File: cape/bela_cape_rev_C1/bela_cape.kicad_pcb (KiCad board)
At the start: 4 copper layers, 127 parts, among them IC1 TLV320AIC3104, IC2 MIC5317, IC3 ES9080Q, IC4 LM4876, IC5 LM4876, IC6 TSV524xIQ4T, IC7 TSV524xIQ4T, IC8 ADS8168, J1 Conn_01x02, J10 Conn_01x04, J11 Conn_01x02, J2 Conn_01x04, J3 Conn_01x03, J4 Conn_01x03, J5 Conn_01x02, J6 Conn_01x02, J7 Conn_01x10, J8 Conn_01x10, J9 Conn_01x04, P1 BeagleBone_Black_Header, U1 TL974, U2 TL974

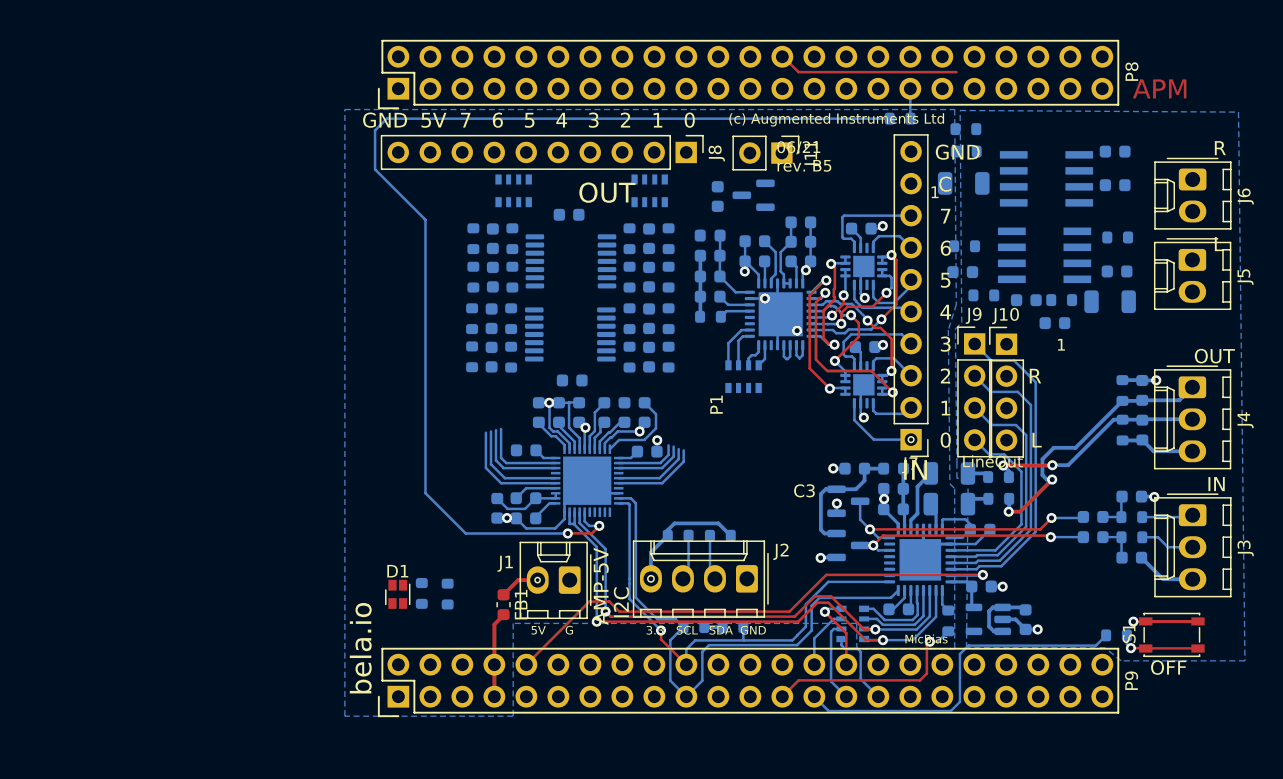
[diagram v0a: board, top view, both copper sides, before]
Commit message: Updates to Bela cape C1, adding 3-pin connectors for raw analog out
(cherry picked from commit eb88a9ebe73bf9c3f735ce6d0fd609408781e91a)
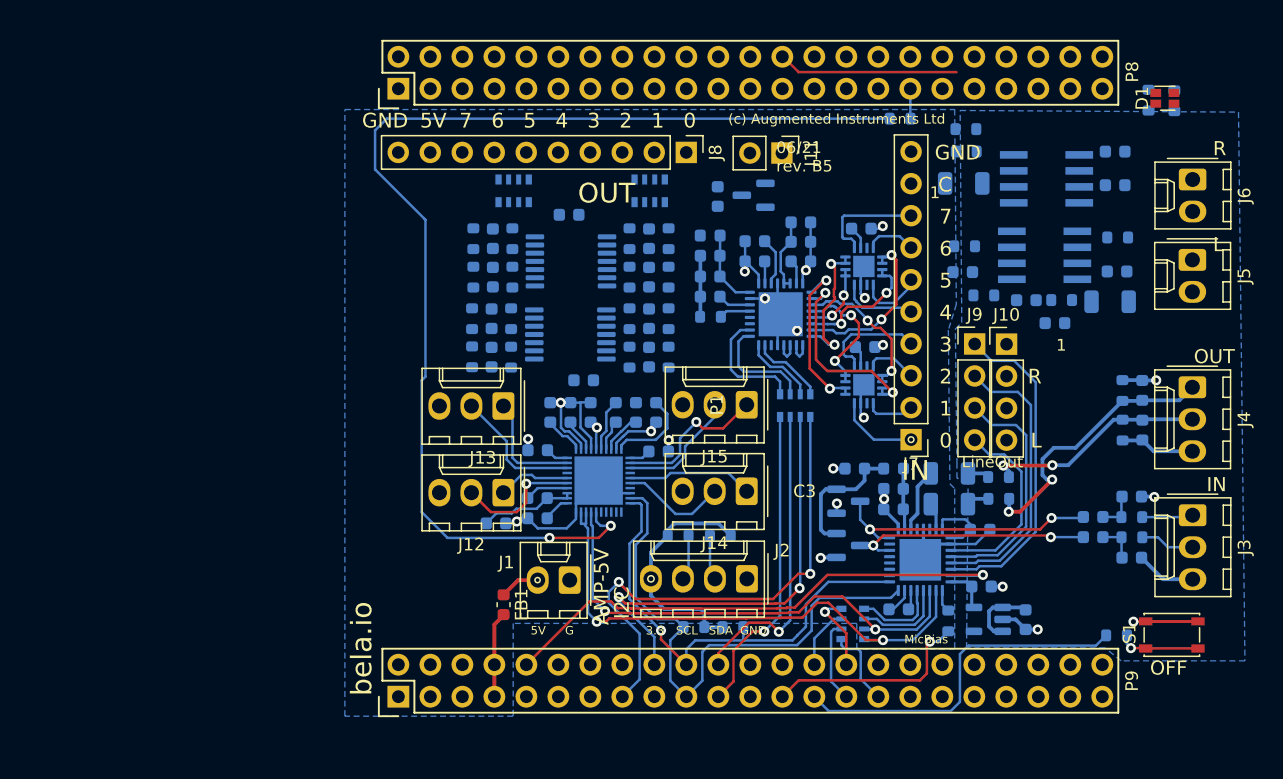
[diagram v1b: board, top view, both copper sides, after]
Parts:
- added J12: Conn_01x03, Connector_Molex:Molex_KK-254_AE-6410-03A_1x03_P2.54mm_Vertical, F.Cu at (125.4, 114.3)
- added J13: Conn_01x03, Connector_Molex:Molex_KK-254_AE-6410-03A_1x03_P2.54mm_Vertical, F.Cu at (125.4, 107.4)
- added J14: Conn_01x03, Connector_Molex:Molex_KK-254_AE-6410-03A_1x03_P2.54mm_Vertical, F.Cu at (144.7, 114.2)
- added J15: Conn_01x03, Connector_Molex:Molex_KK-254_AE-6410-03A_1x03_P2.54mm_Vertical, F.Cu at (144.7, 107.3)
- moved D1 72.5 mm to (177.9, 83.0), turned to 90 degrees
- moved R15 69.7 mm to (178.7, 83.2)
- moved R14 69.7 mm to (176.6, 83.1)
- moved RN2 4.70 mm to (148.6, 107.3)
- moved C19 1.20 mm to (124.8, 116.7), turned to 180 degrees
- moved C42 0.91 mm to (129.1, 107.9)
- moved C46 0.91 mm to (128.1, 110.9)
- moved C35 0.91 mm to (135.9, 107.9)
- moved C37 0.91 mm to (137.7, 111.0)
- moved C43 0.91 mm to (130.7, 107.9)
- moved C44 0.91 mm to (132.3, 107.9)
- moved C45 0.91 mm to (134.3, 107.9)
- moved C47 0.91 mm to (137.5, 107.9)
- moved C48 0.91 mm to (128.1, 114.7)
- moved IC3 0.91 mm to (132.9, 113.3)
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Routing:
- net SPI_ADC_CNV: track 0.00 -> 40.1 mm, vias 0 -> 2
- net SPI_MOSI: track 0.00 -> 35.2 mm, vias 0 -> 2
- net SPI_MISO: track 0.00 -> 24.8 mm, vias 0 -> 1
- net SPI_SCK: track 0.00 -> 24.4 mm, vias 0 -> 1
- net /Analog Output/DAC7: track 4.99 -> 12.3 mm, vias 0 -> 1
- net +3V3: track 32.5 -> 39.8 mm
- net Net-(IC8-Pad25): track 2.99 -> 8.69 mm
- net Net-(IC8-Pad26): track 3.88 -> 9.50 mm
- net /Analog Output/DAC5: track 5.53 -> 9.82 mm
- net Net-(IC8-Pad23): track 1.81 -> 5.95 mm
- net /Analog Output/DAC3: track 6.19 -> 10.0 mm
- net Net-(IC8-Pad24): track 2.11 -> 5.84 mm
- net /Analog Output/DAC4: track 7.39 -> 10.5 mm
- net AUD_DOUT2: track 89.1 -> 91.6 mm
- net /Analog Output/DAC2: track 8.20 -> 5.75 mm
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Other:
- board text removed: "APM"

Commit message: More C1 cape routing
(cherry picked from commit db7d999e21b46c22925661ce0002776775f31ffd)
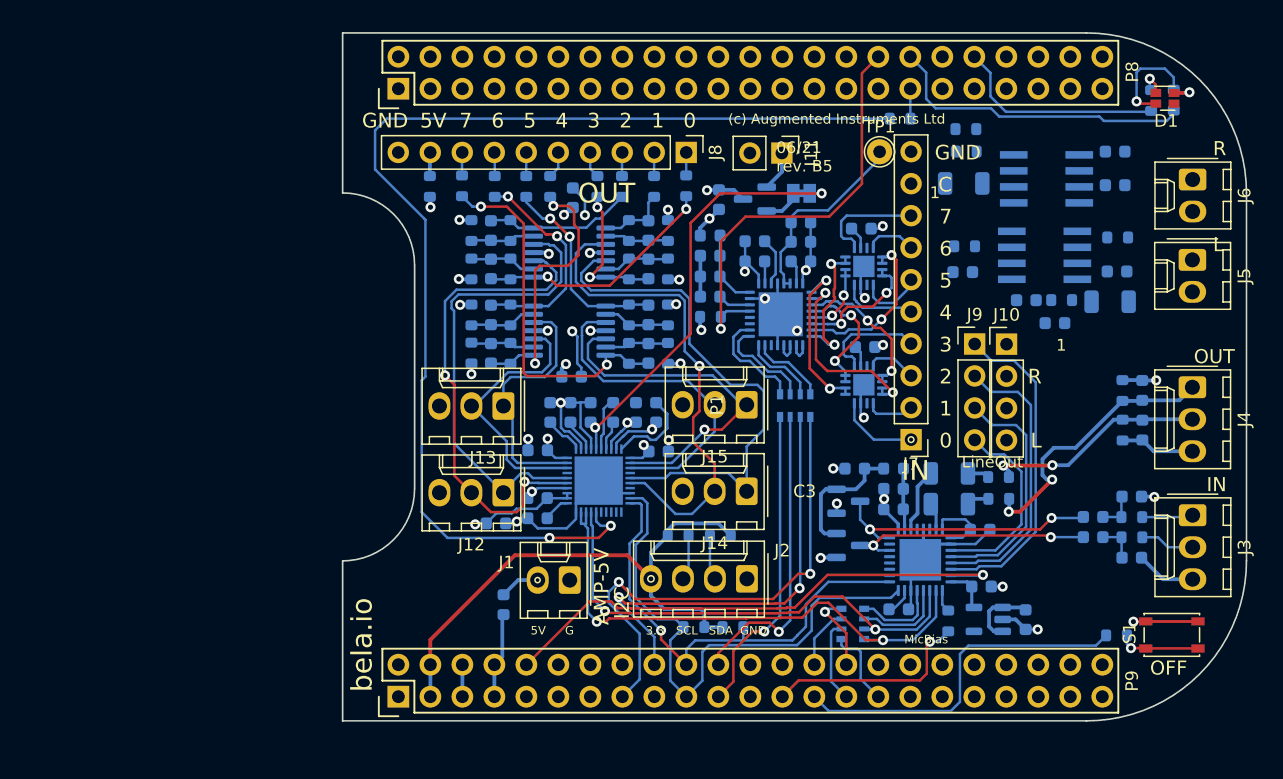
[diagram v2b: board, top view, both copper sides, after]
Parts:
- removed RN3, RN4: 220, Resistor_SMD:R_Array_Convex_4x0603
- added JP1: SolderJumper_2_Bridged, Jumper:SolderJumper-2_P1.3mm_Bridged_Pad1.0x1.5mm, B.Cu at (149.1, 90.5)
- added R39: 220, Resistor_SMD:R_0603_1608Metric, B.Cu at (139.9, 89.9)
- added R40: 220, Resistor_SMD:R_0603_1608Metric, B.Cu at (137.3, 90.0)
- added R41: 220, Resistor_SMD:R_0603_1608Metric, B.Cu at (134.8, 90.0)
- added R42: 220, Resistor_SMD:R_0603_1608Metric, B.Cu at (132.8, 90.0)
- added R43: 220, Resistor_SMD:R_0603_1608Metric, B.Cu at (129.1, 90.0)
- added R44: 220, Resistor_SMD:R_0603_1608Metric, B.Cu at (127.2, 90.0)
- added R45: 220, Resistor_SMD:R_0603_1608Metric, B.Cu at (124.7, 90.0)
- added R46: 220, Resistor_SMD:R_0603_1608Metric, B.Cu at (122.1, 89.9)
- added TP1: TestPoint, TestPoint:TestPoint_THTPad_D2.0mm_Drill1.0mm, F.Cu at (155.2, 87.2)
- FB1: moved to B.Cu
- moved R11 44.8 mm to (119.5, 90.0), turned to 90 degrees
- moved C49 1.38 mm to (130.9, 90.8), turned to -90 degrees
- moved C51 1.00 mm to (130.8, 105.0)
- moved U1 0.71 mm to (130.7, 95.2)
- moved R20 0.67 mm to (122.8, 96.5)
- moved C31 0.67 mm to (124.4, 96.5)
- moved R25 0.67 mm to (126.0, 96.5)
- moved R21 0.67 mm to (122.8, 93.5)
- moved C32 0.67 mm to (124.4, 93.5)
- moved R26 0.67 mm to (126.0, 93.5)
- moved R24 0.65 mm to (138.4, 96.5)
- moved R28 0.65 mm to (135.3, 96.5)
- moved C34 0.65 mm to (136.9, 96.5)
- moved R22 0.65 mm to (138.4, 93.5)
- moved R27 0.65 mm to (135.3, 93.5)
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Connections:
- C1 pad 2: GND -> GNDA
- C13 pad 1: GND -> GNDA
- C18 pad 1: GND -> GNDA
- C19 pad 1: GNDD -> GND
- C2 pad 2: GND -> GNDA
- C22 pad 1: GND -> GNDA
- C23 pad 1: GND -> GNDA
- C24 pad 1: GND -> GNDA
- C25 pad 1: GND -> GNDA
- C26 pad 2: GND -> GNDA
- C27 pad 2: GND -> GNDA
- C28 pad 2: GND -> GNDA
- C29 pad 2: GND -> GNDA
- C3 pad 2: GND -> GNDA
- C30 pad 2: GND -> GNDA
- C32 pad 1: /Analog Output/ANALOG_OUT1 -> /Analog Output/ANALOG_OUT2
- C33 pad 1: /Analog Output/ANALOG_OUT2 -> /Analog Output/ANALOG_OUT1
- C35 pad 1: GNDD -> GND
- C38 pad 1: /Analog Output/ANALOG_OUT5 -> /Analog Output/ANALOG_OUT6
- C4 pad 2: GND -> GNDA
- C40 pad 1: /Analog Output/ANALOG_OUT6 -> /Analog Output/ANALOG_OUT5
- C41 pad 1: GNDD -> GND
- C5 pad 2: GND -> GNDA
- C52 pad 2: GND -> GNDA
- C53 pad 1: GND -> GNDA
- C6 pad 2: GND -> GNDA
- D2 pad 2: /Analog Output/PNEG -> Net-(D2-Pad2)
- D5 pad 1: GND -> GNDA
- D6 pad 1: GND -> GNDA
- D7 pad 1: GND -> GNDA
- D8 pad 1: GND -> GNDA
- IC1 pad 17: GND -> GNDA
- IC1 pad 21: GND -> GNDA
- IC1 pad 26: GND -> GNDA
- IC1 pad 33: GND -> GNDA
- IC1 pad 6: GND -> GNDA
- IC2 pad 2: GND -> GNDA
- IC3 pad 28: GNDD -> GND
- IC3 pad 40: GNDD -> GND
- IC3 pad 41: GNDD -> GND
- IC6 pad 11: GND -> GNDA
- IC6 pad 17: GND -> GNDA
- IC7 pad 11: GND -> GNDA
- IC7 pad 17: GND -> GNDA
- IC8 pad 1: GND -> GNDA
- IC8 pad 21: GND -> GNDA
- IC8 pad 31: GND -> GNDA
- IC8 pad 33: GND -> GNDA
- IC8 pad 4: GND -> GNDA
- IC8 pad 8: GND -> unconnected-(IC8-Pad8)
- J10 pad 1: GND -> GNDA
- J10 pad 3: GND -> GNDA
- J11 pad 2: GNDA -> GND
- J3 pad 3: GND -> GNDA
- J4 pad 3: GND -> GNDA
- J7 pad 10: /Analog Input/REFP -> GNDA
- J7 pad 9: GND -> GNDA
- P1 pad P8.34: unconnected-(P1-PadP8.34) -> /LED0
- P1 pad P8.38: unconnected-(P1-PadP8.38) -> /LED1
- R14 pad 1: unconnected-(R14-Pad1) -> /LED1
- R15 pad 2: unconnected-(R15-Pad2) -> /LED0
- R26 pad 2: /Analog Output/ANALOG_OUT1 -> /Analog Output/ANALOG_OUT2
- R27 pad 2: /Analog Output/ANALOG_OUT2 -> /Analog Output/ANALOG_OUT1
- R3 pad 1: GND -> GNDA
- R34 pad 2: /Analog Output/ANALOG_OUT5 -> /Analog Output/ANALOG_OUT6
- R36 pad 2: /Analog Output/ANALOG_OUT6 -> /Analog Output/ANALOG_OUT5
- R4 pad 1: GND -> GNDA
- U1 pad 10: /Analog Output/DAC2 -> /Analog Output/DAC1
- U1 pad 5: /Analog Output/DAC1 -> /Analog Output/DAC2
- U1 pad 7: /Analog Output/ANALOG_OUT1 -> /Analog Output/ANALOG_OUT2
- U1 pad 8: /Analog Output/ANALOG_OUT2 -> /Analog Output/ANALOG_OUT1
- U2 pad 10: /Analog Output/DAC6 -> /Analog Output/DAC5
- U2 pad 5: /Analog Output/DAC5 -> /Analog Output/DAC6
- U2 pad 7: /Analog Output/ANALOG_OUT5 -> /Analog Output/ANALOG_OUT6
- U2 pad 8: /Analog Output/ANALOG_OUT6 -> /Analog Output/ANALOG_OUT5
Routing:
- net GNDA: track 22.4 -> 103.2 mm, vias 4 -> 29
- net +5V: track 6.82 -> 68.0 mm, vias 0 -> 6
- net GND: track 77.7 -> 40.5 mm, vias 17 -> 4
- net Net-(C49-Pad1): track 0.00 -> 34.9 mm, vias 0 -> 5
- net /Analog Output/DAC3: track 10.0 -> 41.7 mm
- net ADC_DAC_EN: track 2.49 -> 34.1 mm, vias 0 -> 1
- net /Analog Output/PNEG: track 2.53 -> 34.1 mm, vias 1 -> 2
- net /Analog Output/DAC2: track 5.75 -> 37.0 mm
- net /Analog Output/DAC1: track 8.47 -> 39.2 mm, vias 0 -> 1
- net /Analog Output/ANALOG_OUT7: track 0.00 -> 29.2 mm, vias 0 -> 2
- net /Analog Output/DAC0: track 10.1 -> 38.7 mm, vias 1 -> 2
- net +3V3: track 39.8 -> 65.3 mm
- net /LED0: track 0.00 -> 24.7 mm
- net /Analog Output/ANALOG_OUT4: track 0.00 -> 22.0 mm, vias 0 -> 2
- net /Analog Output/ANALOG_OUT0: track 0.00 -> 19.5 mm, vias 0 -> 2
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- added copper zone on In2.Cu, net GND
- added copper zone on In2.Cu, net GNDA
- removed copper zone on B.Cu, net (none)
- removed copper zone on B.Cu, net GND
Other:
- board outline added: 71.8 x 54.6 mm

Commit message: Further routing on C1 cape
(cherry picked from commit 232a25b01e013bf194cdc3a343766aa7b43870aa)
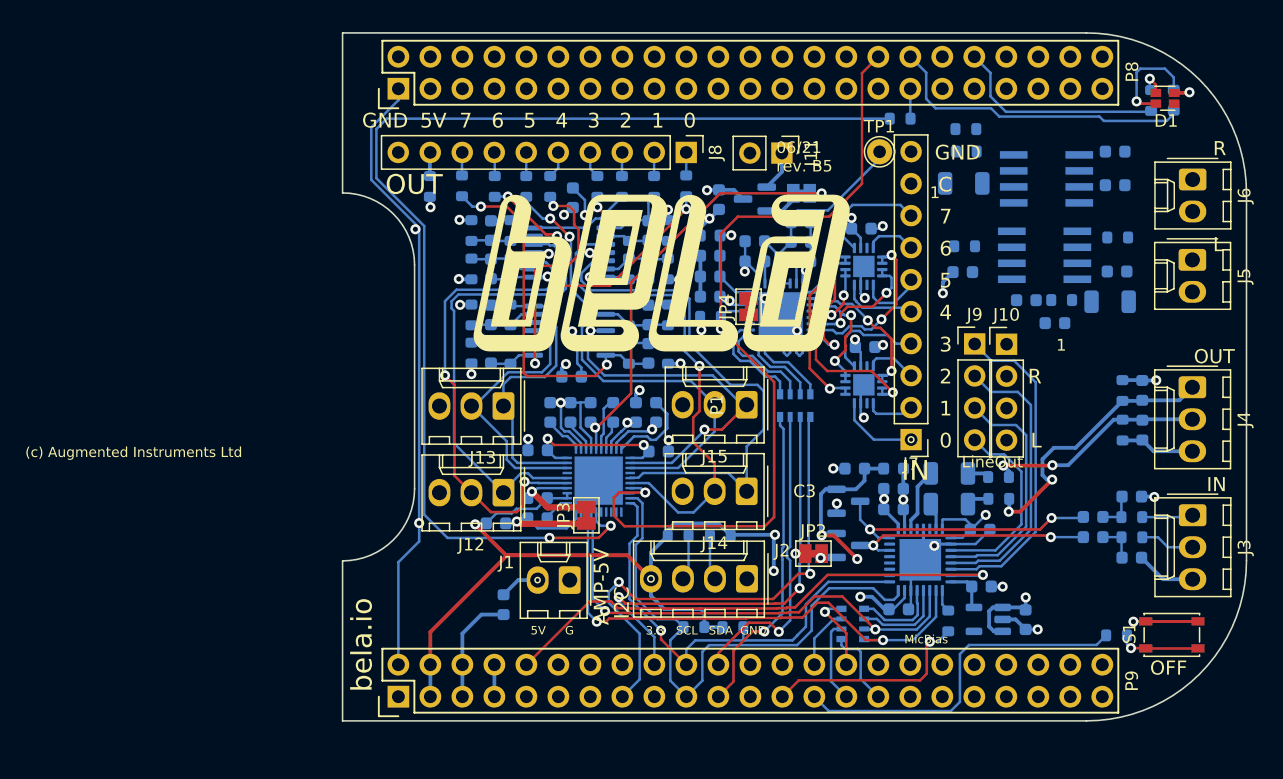
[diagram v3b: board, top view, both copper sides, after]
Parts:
- added G1: Bela-Logo, Bela:Bela-Logo_30mm_Silkscreen, F.Cu at (137.3, 97.0)
- added JP2: SolderJumper_2_Bridged, Jumper:SolderJumper-2_P1.3mm_Bridged_Pad1.0x1.5mm, F.Cu at (150.0, 119.1)
- added JP3: SolderJumper_2_Bridged, Jumper:SolderJumper-2_P1.3mm_Bridged_Pad1.0x1.5mm, F.Cu at (132.0, 116.0)
- added JP4: SolderJumper_2_Bridged, Jumper:SolderJumper-2_P1.3mm_Bridged_Pad1.0x1.5mm, F.Cu at (144.8, 99.5)
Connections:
- C19 pad 2: +3.3V -> +3V3
- C35 pad 1: GND -> GNDA
- C35 pad 2: +3.3V -> +3V3
- C37 pad 2: +3.3V -> +3V3
- C46 pad 2: +3.3V -> +3V3
- C48 pad 2: +3.3V -> +3V3
- FB1 pad 2: +5V -> +5VP
- IC3 pad 10: +3.3V -> +3V3
- IC3 pad 18: +3.3V -> +3V3
- IC3 pad 2: +3.3V -> +3V3
- IC3 pad 21: +3.3V -> +3V3
- IC3 pad 3: +3.3V -> +3V3
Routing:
- net +3V3: track 65.3 -> 178.4 mm, vias 0 -> 11
- net GND: track 40.5 -> 96.1 mm, vias 4 -> 7
- net +5V_AMP: track 3.19 -> 55.0 mm, vias 0 -> 1
- net +5V: track 68.0 -> 113.4 mm
- net ADC_DAC_EN: track 34.1 -> 70.0 mm, vias 1 -> 2
- net +3.3V: track 32.6 -> 0.00 mm, vias 4 -> 0
- net /Analog Input/5V_ANALOG: track 9.70 -> 32.7 mm, vias 0 -> 3
- net +3.3VA: track 10.2 -> 19.0 mm, vias 0 -> 2
- net +5VP: track 2.54 -> 8.90 mm
- net GNDA: track 103.2 -> 109.1 mm, vias 29 -> 31
- net /Analog Input/ANALOG7: track 8.65 -> 9.23 mm
- net SDA: track 37.6 -> 37.0 mm
- net Net-(IC6-Pad15): track 10.3 -> 9.78 mm
